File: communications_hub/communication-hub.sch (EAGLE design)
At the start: 43 parts, among them CON1 SM04B-GHS-TB, CON2 SM04B-GHS-TB, CON3 SM03B-GHS-TB, CON4 SM03B-GHS-TB, CON5 SM02B-GHS-TB, U3 TCAN1042HVDR, U4 TCAN1042HVDR

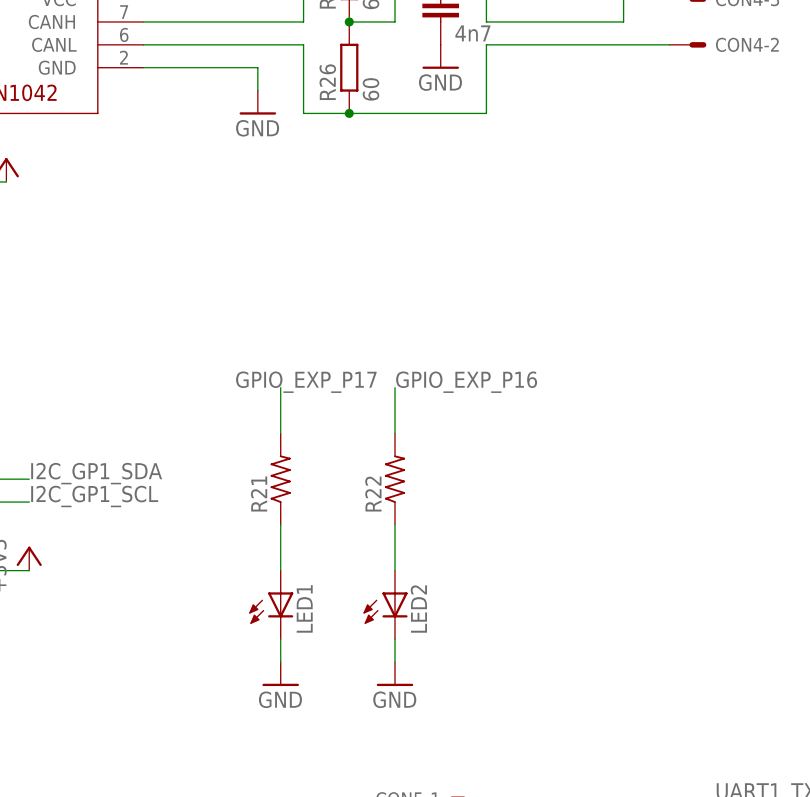
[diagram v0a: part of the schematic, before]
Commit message: Changed folder structure
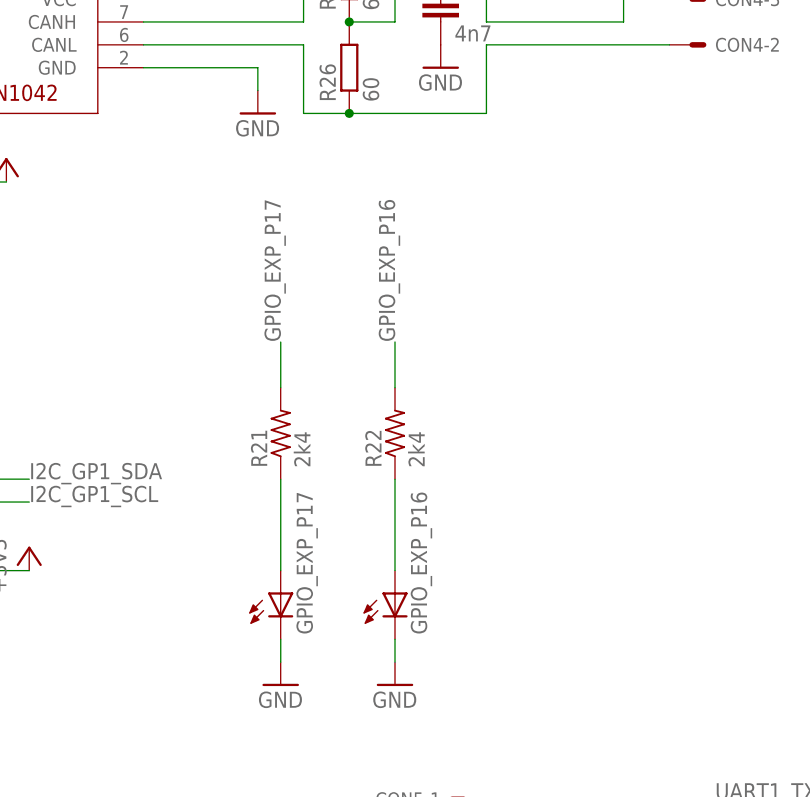
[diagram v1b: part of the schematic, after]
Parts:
- R21, R22: value (none) -> 2k4
- renumbered LED1 to GPIO_EXP_P17, LED2 to GPIO_EXP_P16
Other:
- moved on the sheet: R21, R22
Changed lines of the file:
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@@
 <?xml version="1.0" encoding="utf-8"?>
 <!DOCTYPE eagle SYSTEM "eagle.dtd">
-<eagle version="8.4.1">
+<eagle version="8.4.3">
 <drawing>
 <settings>
@@
 <layer number="56" name="wert" color="7" fill="1" visible="no" active="no"/>
 <layer number="57" name="tCAD" color="7" fill="1" visible="no" active="no"/>
-<layer number="88" name="SimResults" color="9" fill="1" visible="yes" active="yes"/>
-<layer number="89" name="SimProbes" color="9" fill="1" visible="yes" active="yes"/>
+<layer number="88" name="SimResults" color="9" fill="1" visible="no" active="yes"/>
+<layer number="89" name="SimProbes" color="9" fill="1" visible="no" active="yes"/>
 <layer number="90" name="Modules" color="5" fill="1" visible="yes" active="yes"/>
 <layer number="91" name="Nets" color="2" fill="1" visible="yes" active="yes"/>
@@
 <layer number="97" name="Info" color="7" fill="1" visible="yes" active="yes"/>
 <layer number="98" name="Guide" color="6" fill="1" visible="yes" active="yes"/>
-<layer number="99" name="SpiceOrder" color="5" fill="1" visible="yes" active="yes"/>
+<layer number="99" name="SpiceOrder" color="5" fill="1" visible="no" active="yes"/>
 <layer number="100" name="Muster" color="7" fill="1" visible="yes" active="yes"/>
 <layer number="101" name="Patch_Top" color="12" fill="4" visible="yes" active="yes"/>
@@
 <part name="R10" library="resistor" library_urn="urn:adsk.eagle:library:348" deviceset="R-US_" device="M1206" package3d_urn="urn:adsk.eagle:package:26088/1"/>
 <part name="+3V10" library="supply1" library_urn="urn:adsk.eagle:library:371" deviceset="+3V3" device=""/>
-<part name="LED1" library="eagle-ltspice" library_urn="urn:adsk.eagle:library:217" deviceset="LED_E" device="" package3d_urn="urn:adsk.eagle:package:13319/1"/>
-<part name="LED2" library="eagle-ltspice" library_urn="urn:adsk.eagle:library:217" deviceset="LED_E" device="" package3d_urn="urn:adsk.eagle:package:13319/1"/>
+<part name="GPIO_EXP_P17" library="eagle-ltspice" library_urn="urn:adsk.eagle:library:217" deviceset="LED_E" device="" package3d_urn="urn:adsk.eagle:package:13319/1"/>
+<part name="GPIO_EXP_P16" library="eagle-ltspice" library_urn="urn:adsk.eagle:library:217" deviceset="LED_E" device="" package3d_urn="urn:adsk.eagle:package:13319/1"/>
 <part name="GND3" library="supply1" library_urn="urn:adsk.eagle:library:371" deviceset="GND" device=""/>
 <part name="GND4" library="supply1" library_urn="urn:adsk.eagle:library:371" deviceset="GND" device=""/>
-<part name="R21" library="resistor" library_urn="urn:adsk.eagle:library:348" deviceset="R-US_" device="M1206" package3d_urn="urn:adsk.eagle:package:26088/1"/>
-<part name="R22" library="resistor" library_urn="urn:adsk.eagle:library:348" deviceset="R-US_" device="M1206" package3d_urn="urn:adsk.eagle:package:26088/1"/>
+<part name="R21" library="resistor" library_urn="urn:adsk.eagle:library:348" deviceset="R-US_" device="M1206" package3d_urn="urn:adsk.eagle:package:26088/1" value="2k4"/>
+<part name="R22" library="resistor" library_urn="urn:adsk.eagle:library:348" deviceset="R-US_" device="M1206" package3d_urn="urn:adsk.eagle:package:26088/1" value="2k4"/>
 <part name="U3" library="ARVP" deviceset="TCAN1042HVDR" device=""/>
 <part name="U4" library="ARVP" deviceset="TCAN1042HVDR" device=""/>
@@
 <instance part="R10" gate="G$1" x="193.04" y="114.3" rot="R270"/>
 <instance part="+3V10" gate="G$1" x="203.2" y="99.06"/>
-<instance part="LED1" gate="G$1" x="231.14" y="93.98"/>
-<instance part="LED2" gate="G$1" x="243.84" y="93.98"/>
+<instance part="GPIO_EXP_P17" gate="G$1" x="231.14" y="93.98"/>
+<instance part="GPIO_EXP_P16" gate="G$1" x="243.84" y="93.98"/>
 <instance part="GND3" gate="1" x="231.14" y="83.82"/>
 <instance part="GND4" gate="1" x="243.84" y="83.82"/>
-<instance part="R21" gate="G$1" x="231.14" y="106.68" rot="R90"/>
-<instance part="R22" gate="G$1" x="243.84" y="106.68" rot="R90"/>
+<instance part="R21" gate="G$1" x="231.14" y="111.76" rot="R90"/>
+<instance part="R22" gate="G$1" x="243.84" y="111.76" rot="R90"/>
 <instance part="U3" gate="G$1" x="200.66" y="195.58"/>
 <instance part="U4" gate="G$1" x="200.66" y="154.94"/>
@@
 <net name="GND" class="0">
 <segment>
-<pinref part="LED1" gate="G$1" pin="C"/>
+<pinref part="GPIO_EXP_P17" gate="G$1" pin="C"/>
 <pinref part="GND3" gate="1" pin="GND"/>
 <wire x1="231.14" y1="88.9" x2="231.14" y2="86.36" width="0.1524" layer="91"/>
 </segment>
 <segment>
-<pinref part="LED2" gate="G$1" pin="C"/>
+<pinref part="GPIO_EXP_P16" gate="G$1" pin="C"/>
 <pinref part="GND4" gate="1" pin="GND"/>
 <wire x1="243.84" y1="88.9" x2="243.84" y2="86.36" width="0.1524" layer="91"/>
@@
 <net name="N$3" class="0">
 <segment>
-<pinref part="LED1" gate="G$1" pin="A"/>
+<pinref part="GPIO_EXP_P17" gate="G$1" pin="A"/>
 <pinref part="R21" gate="G$1" pin="1"/>
-<wire x1="231.14" y1="96.52" x2="231.14" y2="101.6" width="0.1524" layer="91"/>
+<wire x1="231.14" y1="96.52" x2="231.14" y2="106.68" width="0.1524" layer="91"/>
 </segment>
 </net>
 <net name="N$4" class="0">
 <segment>
-<pinref part="LED2" gate="G$1" pin="A"/>
+<pinref part="GPIO_EXP_P16" gate="G$1" pin="A"/>
 <pinref part="R22" gate="G$1" pin="1"/>
-<wire x1="243.84" y1="96.52" x2="243.84" y2="101.6" width="0.1524" layer="91"/>
+<wire x1="243.84" y1="96.52" x2="243.84" y2="106.68" width="0.1524" layer="91"/>
 </segment>
 </net>
@@
 <segment>
 <pinref part="R21" gate="G$1" pin="2"/>
-<wire x1="231.14" y1="116.84" x2="231.14" y2="111.76" width="0.1524" layer="91"/>
-<label x="226.06" y="116.84" size="1.778" layer="95"/>
+<wire x1="231.14" y1="121.92" x2="231.14" y2="116.84" width="0.1524" layer="91"/>
+<label x="231.14" y="121.92" size="1.778" layer="95" rot="R90"/>
 </segment>
 <segment>
@@
 <segment>
 <pinref part="R22" gate="G$1" pin="2"/>
-<wire x1="243.84" y1="116.84" x2="243.84" y2="111.76" width="0.1524" layer="91"/>
-<label x="243.84" y="116.84" size="1.778" layer="95"/>
-</segment>
-<segment>
+<wire x1="243.84" y1="121.92" x2="243.84" y2="116.84" width="0.1524" layer="91"/>
+<label x="243.84" y="121.92" size="1.778" layer="95" rot="R90"/>
+</segment>
+<segment>

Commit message: Added CAM files
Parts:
- removed R22: 2k4, resistor:R-US_M1206
- removed R24, R25, R26: 60, resistor:R-EU_R1206
- added R11, R12: (no value), resistor:R-US_M1206
- added R3: 1k, resistor:R-EU_R0805
- added R4: 220, resistor:R-EU_R0805
- CON3: value SM03B-GHS-TB -> SM02B-GHS-TB; device ARVP:SM03B-GHS-TB -> ARVP:SM02B-GHS-TB
- CON5: value SM02B-GHS-TB -> SM03B-GHS-TB; device ARVP:SM02B-GHS-TB -> ARVP:SM03B-GHS-TB
- R1, R2: value 10k -> 220
- R15, R16: value 220 -> 60; device resistor:R-EU_R0805 -> resistor:R-EU_R1206
- R17: value 1k -> 60; device resistor:R-EU_R0805 -> resistor:R-EU_R1206
- R18: value 220 -> 2k4; device resistor:R-EU_R0805 -> resistor:R-US_M1206
- R7, R8: value (none) -> 10k; device resistor:R-US_M1206 -> resistor:R-EU_R0805
- renumbered C10 to C1, C11 to C5, C12 to C6, C7 to C3, C8 to C4, C9 to C2, J21 to JP21, J26 to JP26, JP1 to JP7, JP2 to JP8, R19 to R5, R20 to R6, R21 to R13, R23 to R14, SJ3 to SJ2, SJ4 to SJ1, U3 to U1, U4 to U2
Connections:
- net CAN0_RX_T: now also R2.1; no longer R16.1
- net CAN0_TX_T: now also R1.1; no longer R15.1
- net CAN1_TX_T: now also R4.1; no longer R18.1
- net GND: now also R7.1, R8.1; no longer R1.1, R2.1
- net GPIO_EXP_P16: now also R18.2; no longer R22.2
- net I2C_GP0_SCL: now also R12.1; no longer R9.1
- net I2C_GP0_SDA: now also R10.1; no longer R8.1
- net I2C_GP1_SCL: now also R11.2; no longer R10.2
- net I2C_GP1_SDA: now also R9.1; no longer R7.1
- net N$1: now also R10.2, R12.2; no longer R8.2, R9.2
- net N$19: now also R15.2; no longer R24.2
- net N$2: now also R11.1, R9.2; no longer R10.1, R7.2
- net N$20: now also R16.1, R17.2; no longer R25.1, R26.2
- net N$21: now also R16.2; no longer R25.2
- net N$22: now also R17.1; no longer R26.1
- net N$23: now also CON5-3.S; no longer CON3-3.S
- net N$24: now also CON5-2.S, R15.1; no longer CON3-2.S, R24.1
- net N$25: now also R1.2; no longer R15.2
- net N$26: now also R2.2; no longer R16.2
- net N$27: now also R3.2, R7.2; no longer R1.2, R17.2
- net N$28: now also R4.2; no longer R18.2
- net N$30: now also R8.2; no longer R2.2
- net N$31: now also CON5-1.S; no longer CON3-1.S
- net N$33: now also JP3.1, R3.1; no longer JP4.1, R17.1
- net N$34: now also JP4.1; no longer JP3.1
- net N$4: now also R18.1; no longer R22.1
- net N$5: now also JP5.1; no longer JP6.1
- net N$6: now also JP6.1; no longer JP5.1
- net UART1_RX: now also CON3-2.S; no longer CON5-2.S
- net UART1_TX: now also CON3-1.S; no longer CON5-1.S
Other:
- moved on the sheet: CON3-1, CON3-2, CON3-TABS, CON5-1, CON5-2, CON5-TABS, JP3, JP4, JP5, JP6, R1, R10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
